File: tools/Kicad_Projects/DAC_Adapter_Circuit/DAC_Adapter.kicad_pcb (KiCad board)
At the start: 2 copper layers, 52 parts, among them P1 CONN_01X05, P2 CONN_01X03, P3 CONN_01X02, P4 CONN_01X02, P5 CONN_01X02, U1 LM324N

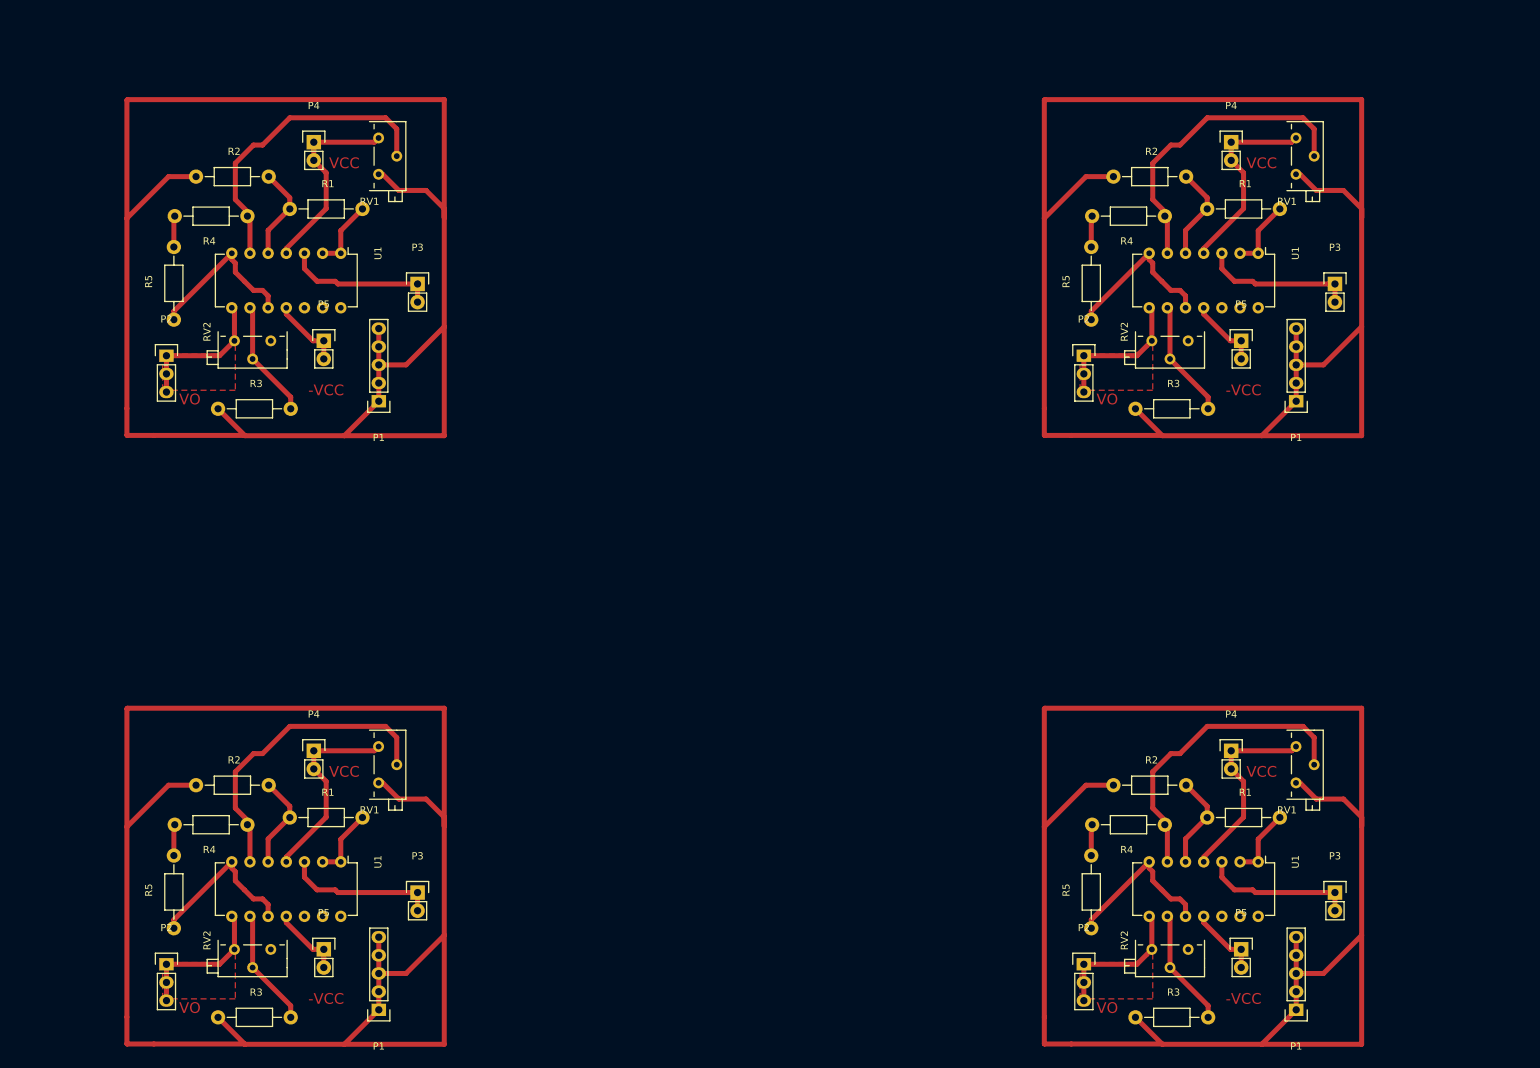
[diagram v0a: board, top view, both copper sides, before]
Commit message: Added clone button functionality
* Also, DAC Adapter Circuit modifications are comitted #34
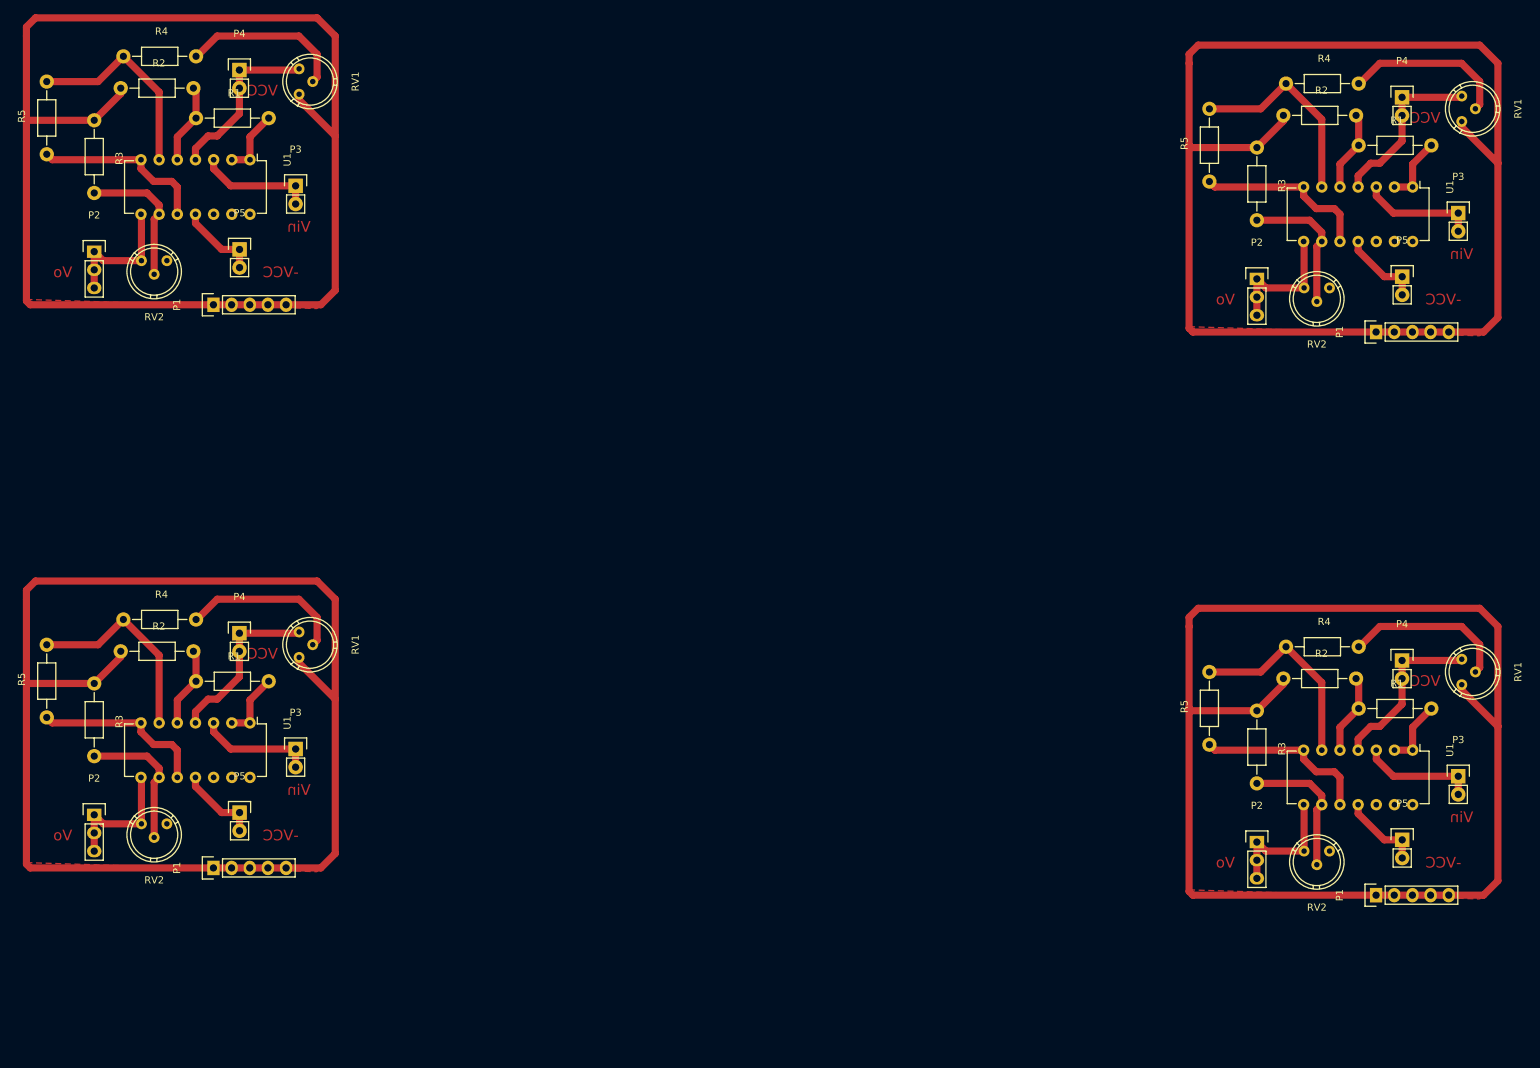
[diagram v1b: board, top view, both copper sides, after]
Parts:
- removed the P1 at (95.0, 81.5)
- removed the P1 at (223.3, 81.5)
- removed the P1 at (223.3, 166.6)
- removed the P1 at (95.0, 166.6)
- removed the P2 at (65.3, 75.2)
- removed the P2 at (193.6, 75.2)
- removed the P2 at (193.6, 160.3)
- removed the P2 at (65.3, 160.3)
- removed the P3 at (100.4, 65.1)
- removed the P3 at (228.7, 65.1)
- removed the P3 at (228.7, 150.2)
- removed the P3 at (100.4, 150.2)
- removed the P4 at (85.9, 45.3)
- removed the P4 at (214.2, 45.3)
- removed the P4 at (214.2, 130.4)
- removed the P4 at (85.9, 130.4)
- removed the P5 at (87.3, 73.1)
- removed the P5 at (215.6, 73.1)
- removed the P5 at (215.6, 158.2)
- removed the P5 at (87.3, 158.2)
- removed the R1 at (82.5, 54.7)
- removed the R1 at (210.8, 54.7)
- removed the R1 at (210.8, 139.7)
- removed the R1 at (82.5, 139.7)
- removed the R2 at (69.4, 50.1)
- removed the R2 at (197.7, 50.1)
- removed the R2 at (197.7, 135.2)
- removed the R2 at (69.4, 135.2)
- removed the R3 at (72.5, 82.6)
- removed the R3 at (200.8, 82.6)
- removed the R3 at (200.8, 167.7)
- removed the R3 at (72.5, 167.7)
- removed the R4 at (76.6, 55.7)
- removed the R4 at (204.9, 55.7)
- removed the R4 at (204.9, 140.7)
- removed the R4 at (76.6, 140.7)
- removed the R5 at (66.3, 70.1)
- removed the R5 at (194.6, 70.1)
- removed the R5 at (194.6, 155.2)
- removed the R5 at (66.3, 155.2)
- removed the RV1 at (95.0, 44.7)
- removed the RV1 at (223.2, 44.7)
- removed the RV1 at (223.2, 129.8)
- removed the RV1 at (95.0, 129.8)
- removed the RV2 at (79.9, 73.1)
- removed the RV2 at (208.2, 73.1)
- removed the RV2 at (208.2, 158.2)
- removed the RV2 at (79.9, 158.2)
- removed the U1 at (89.7, 60.9)
- removed the U1 at (217.9, 60.9)
- removed the U1 at (217.9, 145.9)
- removed the U1 at (89.7, 145.9)
- added P1: CONN_01X05, Pin_Headers:Pin_Header_Straight_1x05, F.Cu at (71.9, 146.8)
- added P1: CONN_01X05, Pin_Headers:Pin_Header_Straight_1x05, F.Cu at (234.4, 150.6)
- added P1: CONN_01X05, Pin_Headers:Pin_Header_Straight_1x05, F.Cu at (234.4, 71.9)
- added P1: CONN_01X05, Pin_Headers:Pin_Header_Straight_1x05, F.Cu at (71.9, 68.1)
- added P2: CONN_01X03, Pin_Headers:Pin_Header_Straight_1x03, F.Cu at (55.2, 139.4)
- added P2: CONN_01X03, Pin_Headers:Pin_Header_Straight_1x03, F.Cu at (217.8, 143.2)
- added P2: CONN_01X03, Pin_Headers:Pin_Header_Straight_1x03, F.Cu at (217.8, 64.4)
- added P2: CONN_01X03, Pin_Headers:Pin_Header_Straight_1x03, F.Cu at (55.2, 60.6)
- added P3: CONN_01X02, Pin_Headers:Pin_Header_Straight_1x02, F.Cu at (83.4, 130.2)
- added P3: CONN_01X02, Pin_Headers:Pin_Header_Straight_1x02, F.Cu at (245.9, 134.0)
- added P3: CONN_01X02, Pin_Headers:Pin_Header_Straight_1x02, F.Cu at (245.9, 55.2)
- added P3: CONN_01X02, Pin_Headers:Pin_Header_Straight_1x02, F.Cu at (83.4, 51.4)
- added P4: CONN_01X02, Pin_Headers:Pin_Header_Straight_1x02, F.Cu at (75.5, 114.0)
- added P4: CONN_01X02, Pin_Headers:Pin_Header_Straight_1x02, F.Cu at (238.1, 117.8)
- added P4: CONN_01X02, Pin_Headers:Pin_Header_Straight_1x02, F.Cu at (238.1, 39.0)
- added P4: CONN_01X02, Pin_Headers:Pin_Header_Straight_1x02, F.Cu at (75.5, 35.2)
- added P5: CONN_01X02, Pin_Headers:Pin_Header_Straight_1x02, F.Cu at (75.5, 139.1)
- added P5: CONN_01X02, Pin_Headers:Pin_Header_Straight_1x02, F.Cu at (238.1, 142.9)
- added P5: CONN_01X02, Pin_Headers:Pin_Header_Straight_1x02, F.Cu at (238.1, 64.1)
- added P5: CONN_01X02, Pin_Headers:Pin_Header_Straight_1x02, F.Cu at (75.5, 60.3)
- added R1: 100k, Resistors_ThroughHole:Resistor_Horizontal_RM10mm, F.Cu at (69.4, 120.7)
- added R1: 100k, Resistors_ThroughHole:Resistor_Horizontal_RM10mm, F.Cu at (232.0, 124.5)
- added R1: 100k, Resistors_ThroughHole:Resistor_Horizontal_RM10mm, F.Cu at (232.0, 45.8)
- added R1: 100k, Resistors_ThroughHole:Resistor_Horizontal_RM10mm, F.Cu at (69.4, 42.0)
- added R2: 100k, Resistors_ThroughHole:Resistor_Horizontal_RM10mm, F.Cu at (58.9, 116.5)
- added R2: 100k, Resistors_ThroughHole:Resistor_Horizontal_RM10mm, F.Cu at (221.5, 120.3)
- added R2: 100k, Resistors_ThroughHole:Resistor_Horizontal_RM10mm, F.Cu at (221.5, 41.6)
- added R2: 100k, Resistors_ThroughHole:Resistor_Horizontal_RM10mm, F.Cu at (58.9, 37.8)
- added R3: 68k, Resistors_ThroughHole:Resistor_Horizontal_RM10mm, F.Cu at (55.2, 121.0)
- added R3: 68k, Resistors_ThroughHole:Resistor_Horizontal_RM10mm, F.Cu at (217.8, 124.8)
- added R3: 68k, Resistors_ThroughHole:Resistor_Horizontal_RM10mm, F.Cu at (217.8, 46.1)
- added R3: 68k, Resistors_ThroughHole:Resistor_Horizontal_RM10mm, F.Cu at (55.2, 42.3)
- added R4: 100k, Resistors_ThroughHole:Resistor_Horizontal_RM10mm, F.Cu at (59.3, 112.1)
- added R4: 100k, Resistors_ThroughHole:Resistor_Horizontal_RM10mm, F.Cu at (221.8, 115.9)
- added R4: 100k, Resistors_ThroughHole:Resistor_Horizontal_RM10mm, F.Cu at (221.8, 37.1)
- added R4: 100k, Resistors_ThroughHole:Resistor_Horizontal_RM10mm, F.Cu at (59.3, 33.3)
- added R5: 100k, Resistors_ThroughHole:Resistor_Horizontal_RM10mm, F.Cu at (48.6, 125.7)
- added R5: 100k, Resistors_ThroughHole:Resistor_Horizontal_RM10mm, F.Cu at (211.1, 129.6)
- added R5: 100k, Resistors_ThroughHole:Resistor_Horizontal_RM10mm, F.Cu at (211.1, 50.8)
- added R5: 100k, Resistors_ThroughHole:Resistor_Horizontal_RM10mm, F.Cu at (48.6, 47.0)
- added RV1: 100k, Potentiometers:Potentiometer_Bourns_3339H_Angular_ScrewUp, F.Cu at (83.8, 113.8)
- added RV1: 100k, Potentiometers:Potentiometer_Bourns_3339H_Angular_ScrewUp, F.Cu at (246.4, 117.6)
- added RV1: 100k, Potentiometers:Potentiometer_Bourns_3339H_Angular_ScrewUp, F.Cu at (246.4, 38.9)
- added RV1: 100k, Potentiometers:Potentiometer_Bourns_3339H_Angular_ScrewUp, F.Cu at (83.8, 35.1)
- added RV2: 100k, Potentiometers:Potentiometer_Bourns_3339H_Angular_ScrewUp, F.Cu at (65.4, 140.6)
- added RV2: 100k, Potentiometers:Potentiometer_Bourns_3339H_Angular_ScrewUp, F.Cu at (227.9, 144.4)
- added RV2: 100k, Potentiometers:Potentiometer_Bourns_3339H_Angular_ScrewUp, F.Cu at (227.9, 65.7)
- added RV2: 100k, Potentiometers:Potentiometer_Bourns_3339H_Angular_ScrewUp, F.Cu at (65.4, 61.9)
- added U1: LM324N, Housings_DIP:DIP-14_W7.62mm, F.Cu at (77.0, 126.5)
- added U1: LM324N, Housings_DIP:DIP-14_W7.62mm, F.Cu at (239.5, 130.3)
- added U1: LM324N, Housings_DIP:DIP-14_W7.62mm, F.Cu at (239.5, 51.6)
- added U1: LM324N, Housings_DIP:DIP-14_W7.62mm, F.Cu at (77.0, 47.8)
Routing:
- net GND: track 968.1 -> 746.6 mm
- net Net-(R4-Pad2): track 17.5 -> 92.9 mm
- net Net-(R4-Pad1): track 172.3 -> 114.8 mm
- net /V1_LBL: track 85.6 -> 65.0 mm
- net +15V: track 111.5 -> 97.0 mm
- net Net-(R3-Pad2): track 65.9 -> 79.0 mm
- net Net-(R1-Pad1): track 52.9 -> 45.0 mm
- net Net-(R5-Pad1): track 92.4 -> 98.8 mm
- net /VO: track 80.9 -> 74.9 mm
- net -15V: track 40.8 -> 45.9 mm
- net Net-(R1-Pad2): track 40.0 -> 37.8 mm
- removed copper zone on F.Cu, net /VO
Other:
- net class Default: clearance 0.7 -> 0.5; trace_width 0.7 -> 1
- rule trace_clearance: 0.7 -> 0.5
- board text added: "Vin"
- board text added: "Vo"
- board text removed: "VO"
